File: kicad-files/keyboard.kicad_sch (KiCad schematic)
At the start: 144 parts

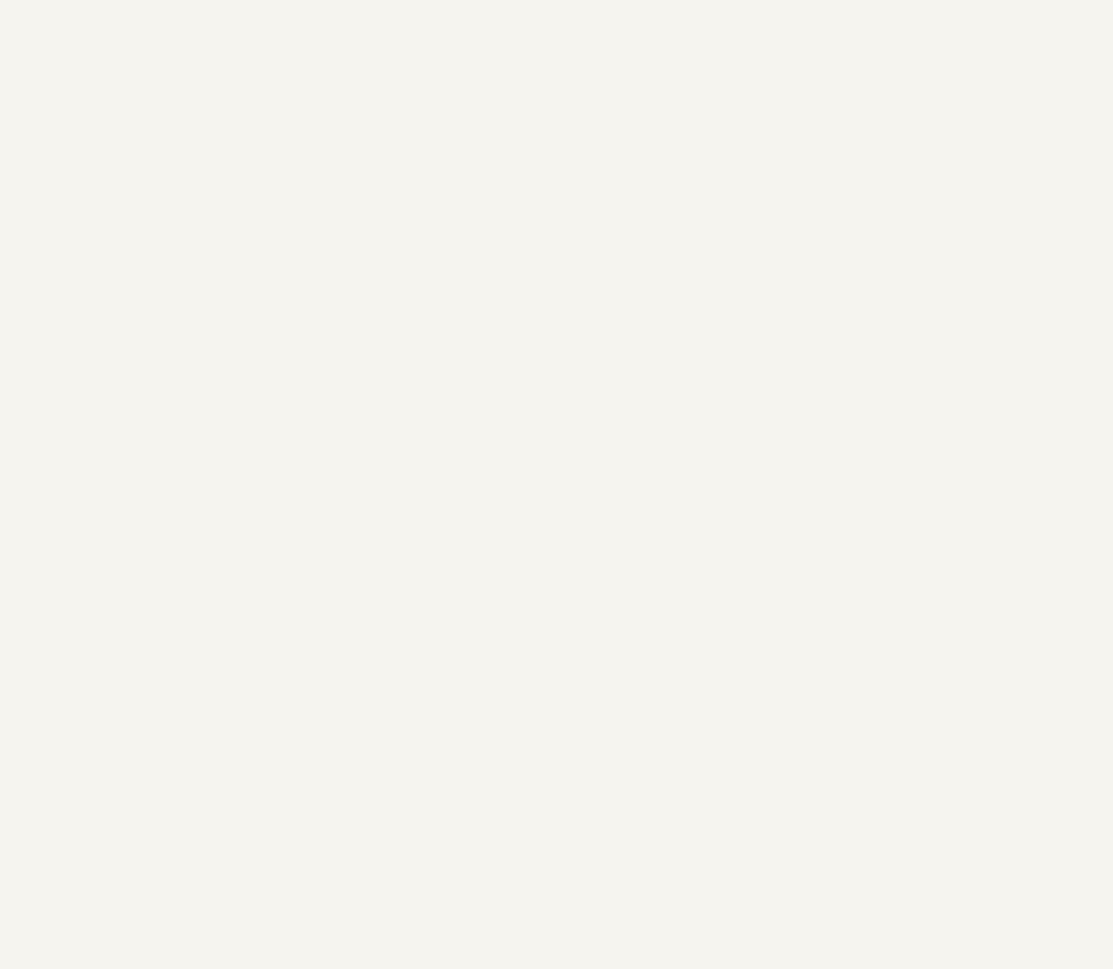
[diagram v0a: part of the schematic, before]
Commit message: Added STM32 micro controller to schematic
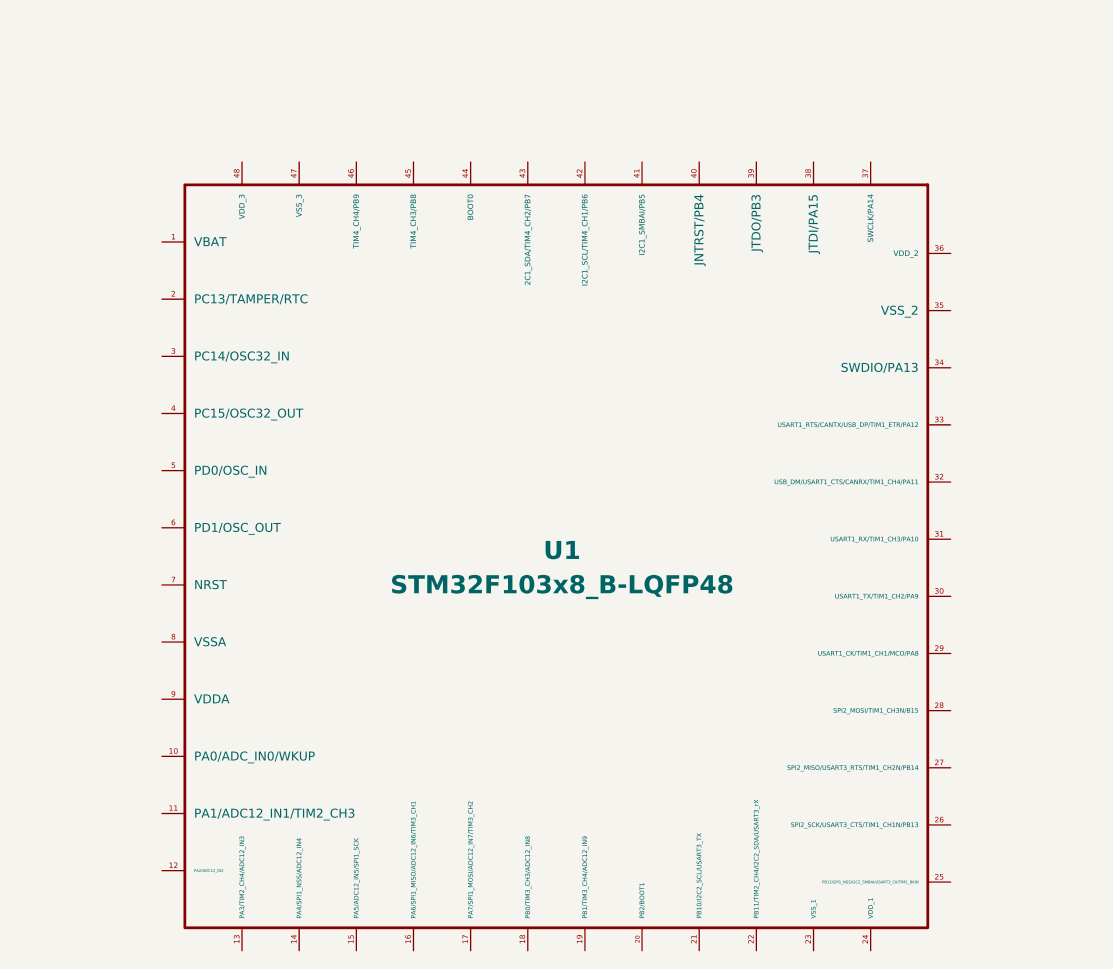
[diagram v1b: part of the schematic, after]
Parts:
- added U1: STM32F103x8_B-LQFP48, acheron_Components:STM_UFQFPN-48_LQFP-48-1EP_7x7mm_P0.5mm_HandSoldering_ThermalReliefs, symbol acheron_Symbols:STM32F103x8_B-LQFP48
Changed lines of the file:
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@@
+    )
+  )
+  (symbol (lib_id "acheron_Symbols:STM32F103x8_B-LQFP48") (at 77.47 234.95 0) (unit 1)
+    (in_bom yes) (on_board yes) (dnp no)
+    (property "Reference" "U1" (at 78.74 233.68 0)
+      (effects (font (size 2.0066 2.0066) bold))
+    )
+    (property "Value" "STM32F103x8_B-LQFP48" (at 78.74 237.49 0)
+      (effects (font (size 2.0066 2.0066) bold))
+    )
+    (property "Footprint" "acheron_Components:STM_UFQFPN-48_LQFP-48-1EP_7x7mm_P0.5mm_HandSoldering_ThermalReliefs" (at 77.47 234.95 0)
+      (effects (font (size 1.27 1.27)) hide)
+    )
+    (property "Datasheet" "" (at 77.47 234.95 0)
+      (effects (font (size 1.27 1.27)) hide)
+    )
+    (pin "1")
+    (pin "10")
+    (pin "11")
+    (pin "12")
+    (pin "13")
+    (pin "14")
+    (pin "15")
+    (pin "16")
+    (pin "17")
+    (pin "18")
+    (pin "19")
+    (pin "2")
+    (pin "20")
+    (pin "21")
+    (pin "22")
+    (pin "23")
+    (pin "24")
+    (pin "25")
+    (pin "26")
+    (pin "27")
+    (pin "28")
+    (pin "29")
+    (pin "3")
+    (pin "30")
+    (pin "31")
+    (pin "32")
+    (pin "33")
+    (pin "34")
+    (pin "35")
+    (pin "36")
+    (pin "37")
+    (pin "38")
+    (pin "39")
+    (pin "4")
+    (pin "40")
+    (pin "41")
+    (pin "42")
+    (pin "43")
+    (pin "44")
+    (pin "45")
+    (pin "46")
+    (pin "47")
+    (pin "48")
+    (pin "5")
+    (pin "6")
+    (pin "7")
+    (pin "8")
+    (pin "9")
+    (instances
+      (project "keyboard"
+        (path "/2fda2561-53ed-4930-8b41-858e0e3dd5f4"
+          (reference "U1") (unit 1)
+        )
+      )
     )
   )

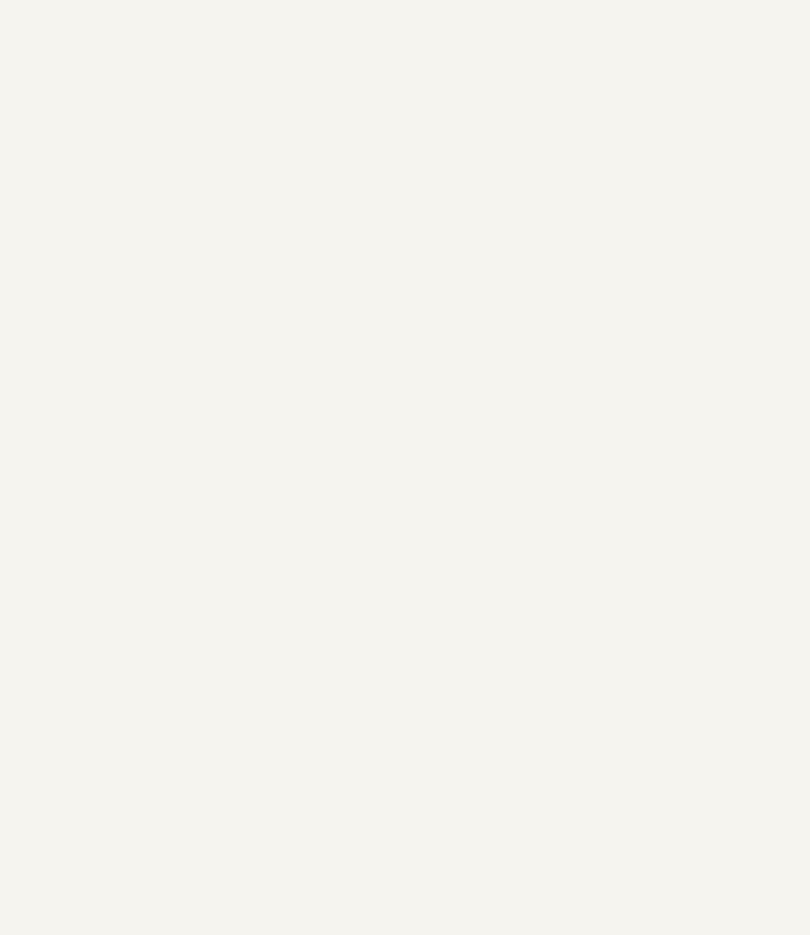
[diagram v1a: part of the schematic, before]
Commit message: Added Type C connector
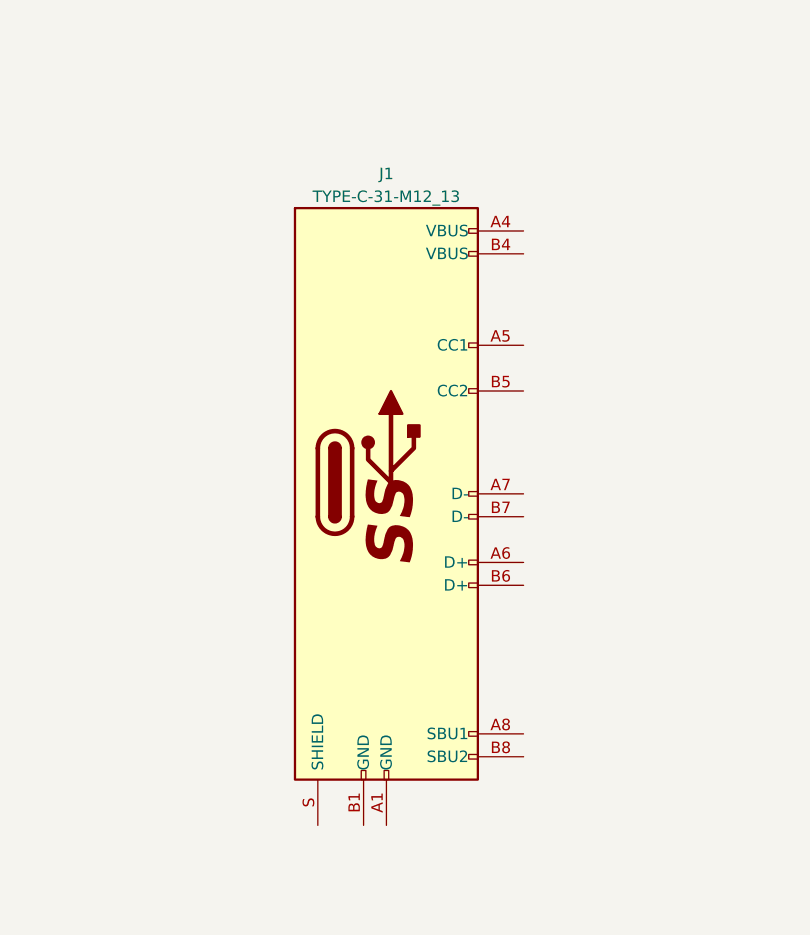
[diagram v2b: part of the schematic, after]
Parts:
- added J1: TYPE-C-31-M12_13, acheron_Connectors:TYPE-C-31-M-12, symbol acheron_Symbols:TYPE-C-31-M12_13
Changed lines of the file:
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@@
+    )
+  )
+  (symbol (lib_id "acheron_Symbols:TYPE-C-31-M12_13") (at 223.52 231.14 0) (unit 1)
+    (in_bom yes) (on_board yes) (dnp no) (fields_autoplaced)
+    (property "Reference" "J1" (at 223.52 195.58 0)
+      (effects (font (size 1.27 1.27)))
+    )
+    (property "Value" "TYPE-C-31-M12_13" (at 223.52 198.12 0)
+      (effects (font (size 1.27 1.27)))
+    )
+    (property "Footprint" "acheron_Connectors:TYPE-C-31-M-12" (at 210.82 229.87 90)
+      (effects (font (size 1.27 1.27)) hide)
+    )
+    (property "Datasheet" "" (at 228.6 229.87 0)
+      (effects (font (size 1.27 1.27)) hide)
+    )
+    (pin "A1")
+    (pin "A4")
+    (pin "A5")
+    (pin "A6")
+    (pin "A7")
+    (pin "A8")
+    (pin "B1")
+    (pin "B4")
+    (pin "B5")
+    (pin "B6")
+    (pin "B7")
+    (pin "B8")
+    (pin "S")
+    (instances
+      (project "keyboard"
+        (path "/2fda2561-53ed-4930-8b41-858e0e3dd5f4"
+          (reference "J1") (unit 1)
+        )
+      )
     )
   )

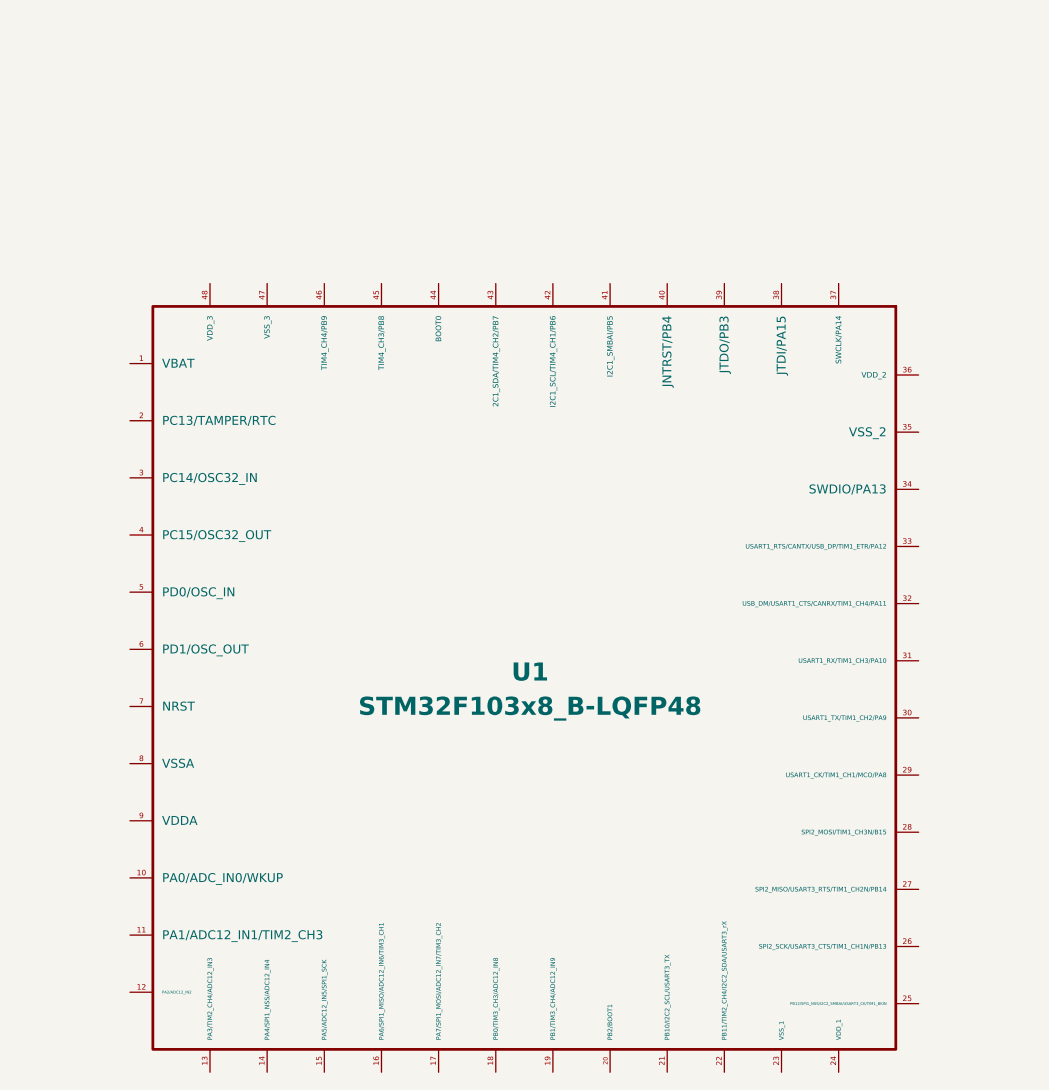
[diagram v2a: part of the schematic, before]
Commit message: Renamed pins on STM
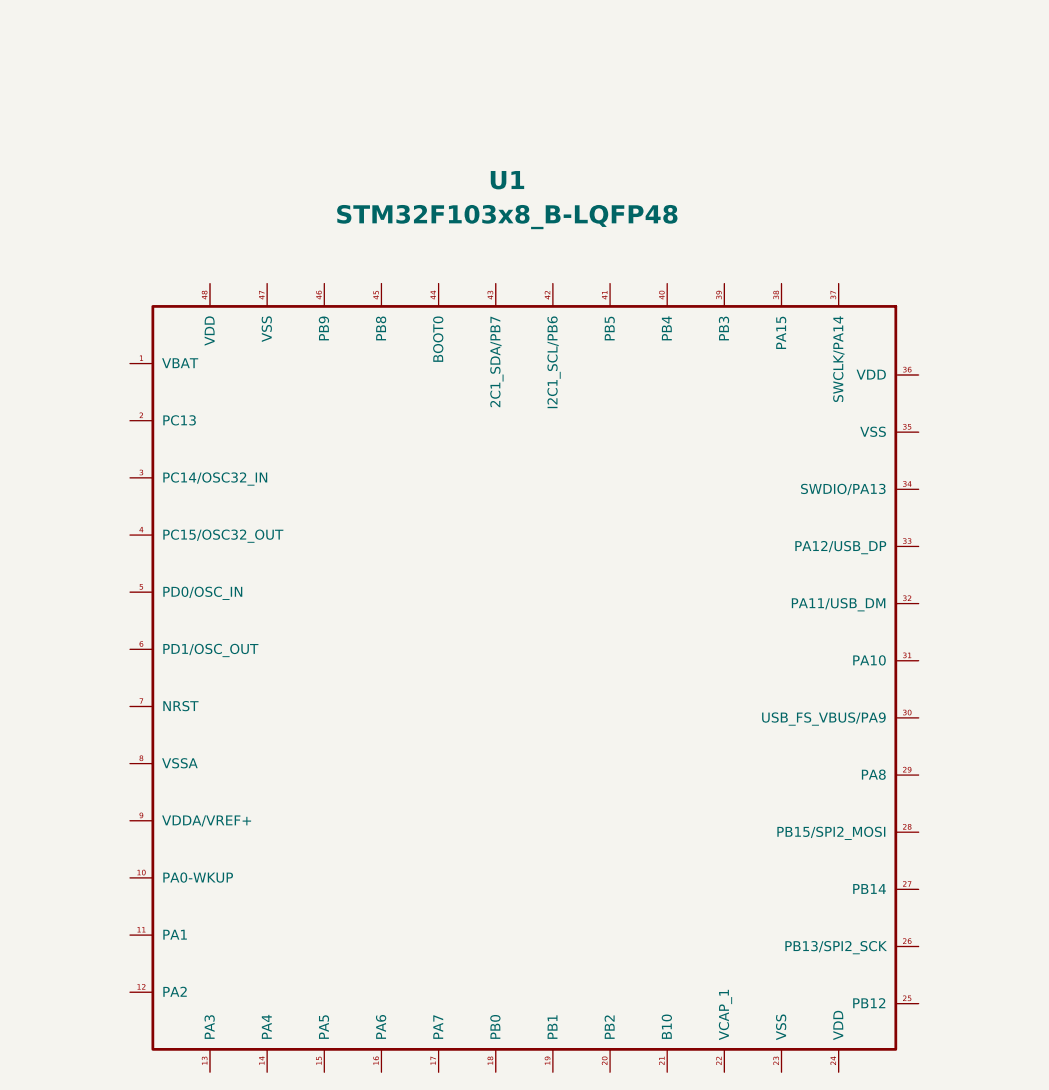
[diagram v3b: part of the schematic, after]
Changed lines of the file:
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@@
   (symbol (lib_id "acheron_Symbols:STM32F103x8_B-LQFP48") (at 77.47 234.95 0) (unit 1)
     (in_bom yes) (on_board yes) (dnp no)
-    (property "Reference" "U1" (at 78.74 233.68 0)
+    (property "Reference" "U1" (at 76.2 179.07 0)
       (effects (font (size 2.0066 2.0066) bold))
     )
-    (property "Value" "STM32F103x8_B-LQFP48" (at 78.74 237.49 0)
+    (property "Value" "STM32F103x8_B-LQFP48" (at 76.2 182.88 0)
       (effects (font (size 2.0066 2.0066) bold))
     )
-    (property "Footprint" "acheron_Components:STM_UFQFPN-48_LQFP-48-1EP_7x7mm_P0.5mm_HandSoldering_ThermalReliefs" (at 77.47 234.95 0)
+    (property "Footprint" "acheron_Components:STM_UFQFPN-48_LQFP-48-1EP_7x7mm_P0.5mm_HandSoldering_ThermalReliefs" (at 77.47 290.83 0)
       (effects (font (size 1.27 1.27)) hide)
     )

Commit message: Swapped switches to cherry MX only & Resized board
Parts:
- K_0, K_1, K_10, K_11, K_12, K_13, K_15, K_17, K_18, K_19, K_2, K_20, K_21, K_22, K_23, K_24, K_25, K_26, K_27, K_28, K_29, K_3, K_30, K_31, K_32, K_33, K_34, K_35, K_36, K_37, K_38, K_39, K_4, K_40, K_41, K_42, K_43, K_44, K_46, K_48, K_49, K_5, K_50, K_51, K_52, K_53, K_54, K_55, K_56, K_57, K_58, K_59, K_6, K_60, K_68, K_69, K_7, K_70, K_71, K_8, K_9: footprint MX_Alps_Hybrid:MX-1U-NoLED -> MX_Only:MXOnly-1U-NoLED
- K_14, K_16, K_47: footprint MX_Alps_Hybrid:MX-2U-NoLED -> MX_Only:MXOnly-2U-NoLED
- K_45, K_65: footprint MX_Alps_Hybrid:MX-3U-NoLED -> MX_Only:MXOnly-3U-NoLED
- K_61: footprint MX_Alps_Hybrid:MX-1.75U-NoLED -> MX_Only:MXOnly-1.75U-NoLED
- K_62, K_63, K_66, K_67: footprint MX_Alps_Hybrid:MX-1.25U-NoLED -> MX_Only:MXOnly-1.25U-NoLED
- K_64: footprint MX_Alps_Hybrid:MX-2.25U-NoLED -> MX_Only:MXOnly-2.25U-NoLED

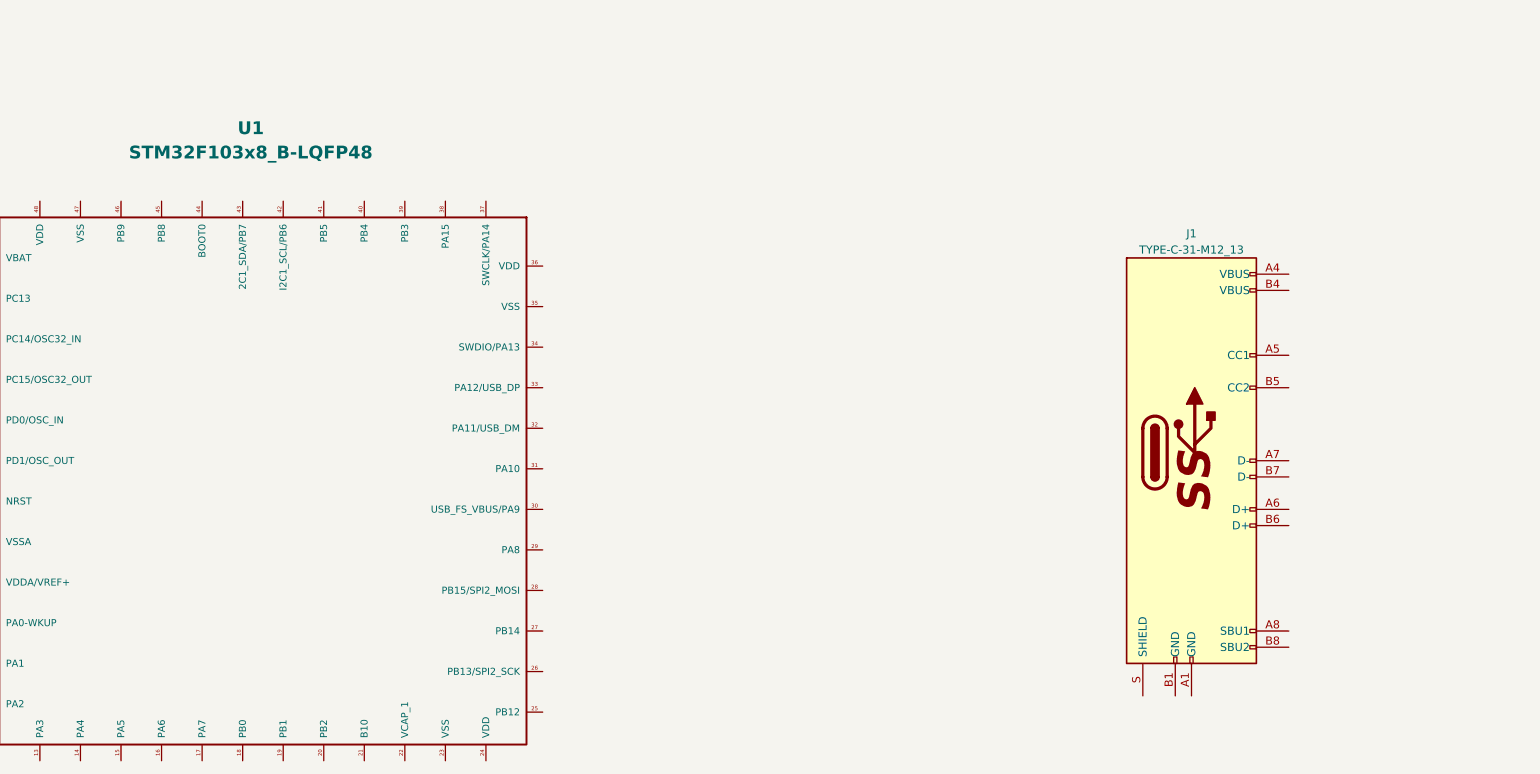
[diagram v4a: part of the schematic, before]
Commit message: Hooked up the Type C connector
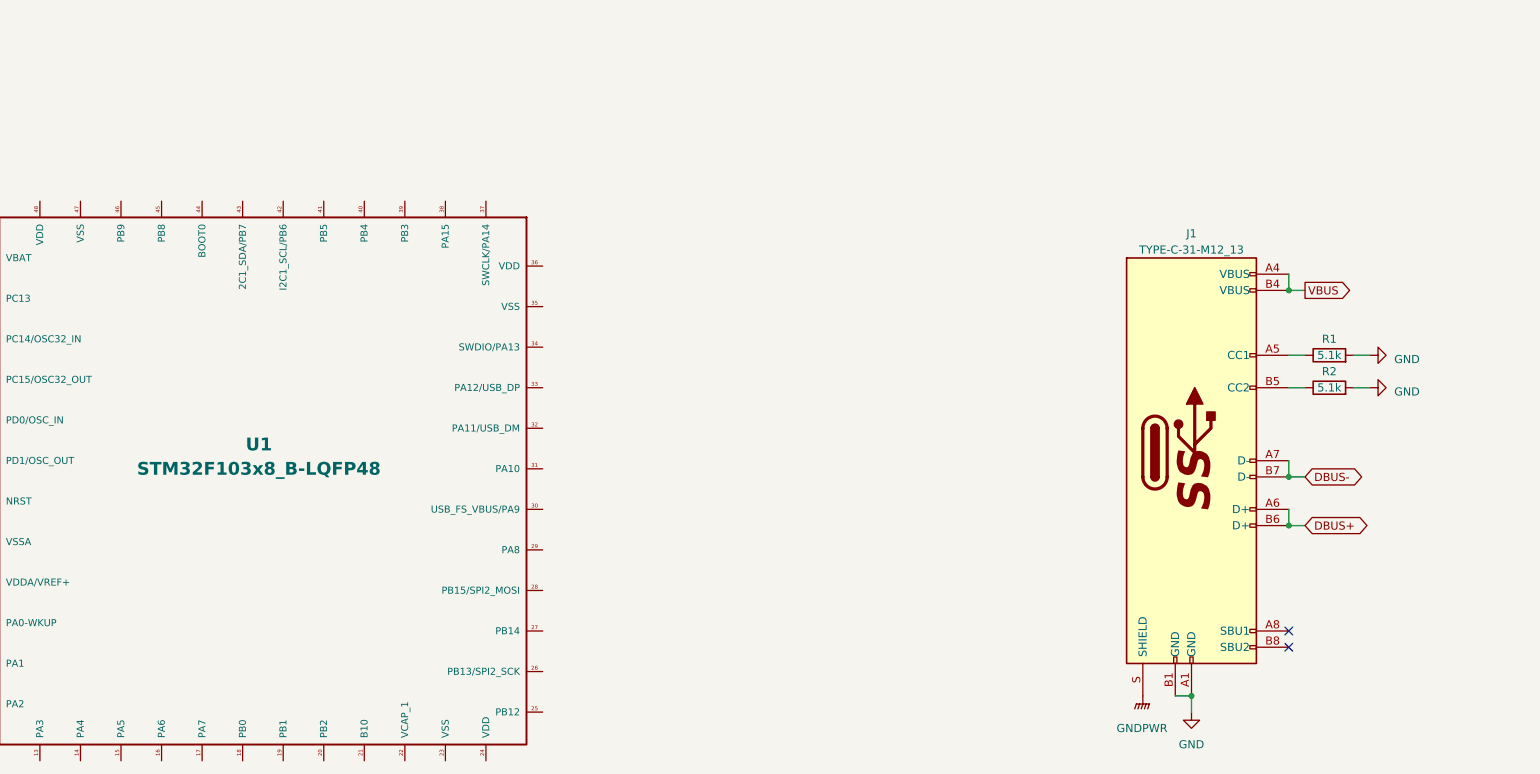
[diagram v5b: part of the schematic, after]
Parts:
- added R1, R2: 5.1k, Resistor_SMD:R_0805_2012Metric, symbol Device:R
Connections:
- net GND: now reaches J1.A1 (GND)
- net GND: now also J1.B1 (GND), R1.2, R2.2
- net VBUS: now reaches J1.A4 (VBUS)
- net VBUS: now also J1.B4 (VBUS)
- net at J1.A5 (CC1): now also R1.1
- net DBUS+: now reaches J1.A6 (D+)
- net DBUS+: now also J1.B6 (D+)
- net DBUS-: now reaches J1.A7 (D-)
- net DBUS-: now also J1.B7 (D-)
- net at J1.B5 (CC2): now also R2.1
- net GNDPWR: now reaches J1.S (SHIELD)
- no-connect marks 0 -> 2
